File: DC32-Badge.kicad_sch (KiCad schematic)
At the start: 37 parts, among them J1 Conn_01x06, J2 Hirose_FH34-SRJ-24S, J3 Conn_01x06, J4 Conn_01x06, J5 Micro_SD_Card_Det, P1 2479, Q1 RTF025N03TL, SW1 SW_Push_DPDT, SW2 SW_Push_DPDT, SW3 SW_Push, SW4 SW_Push, U1 ESP32-C3-MINI-1, U2 AP2112K-3.3

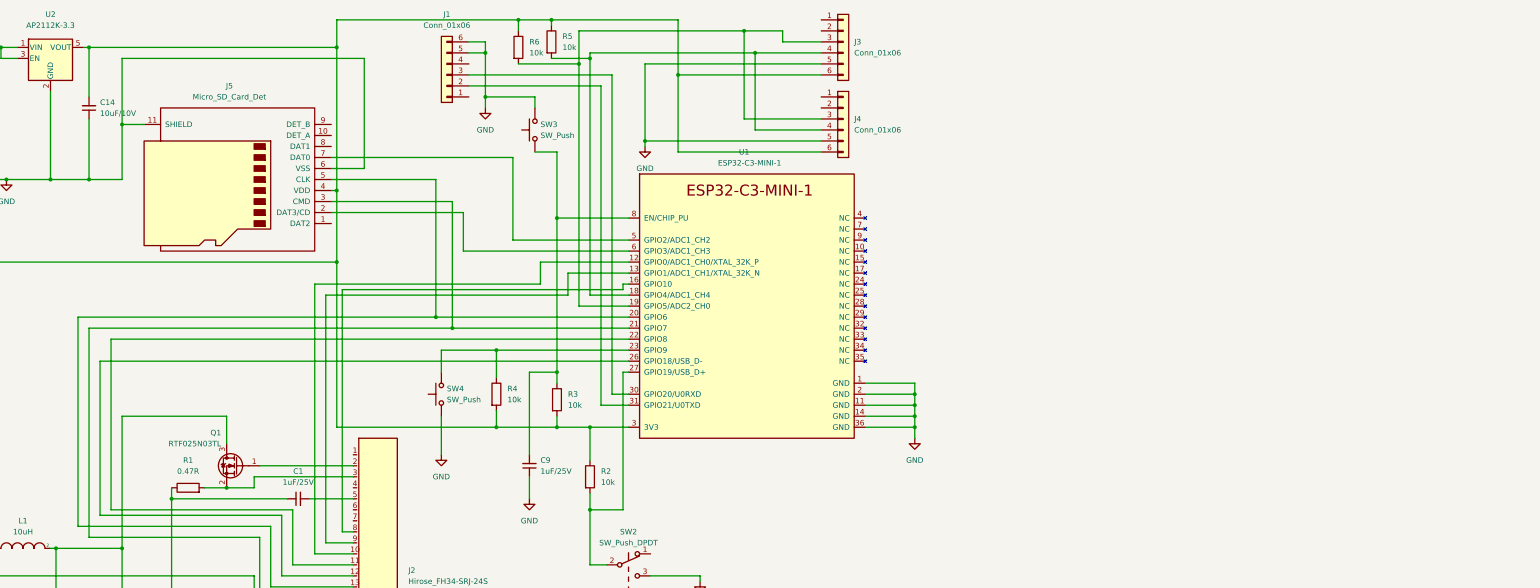
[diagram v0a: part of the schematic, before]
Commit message: Replaced ESP32-MINI with ESP32-WROOM in the kicad_sch file.
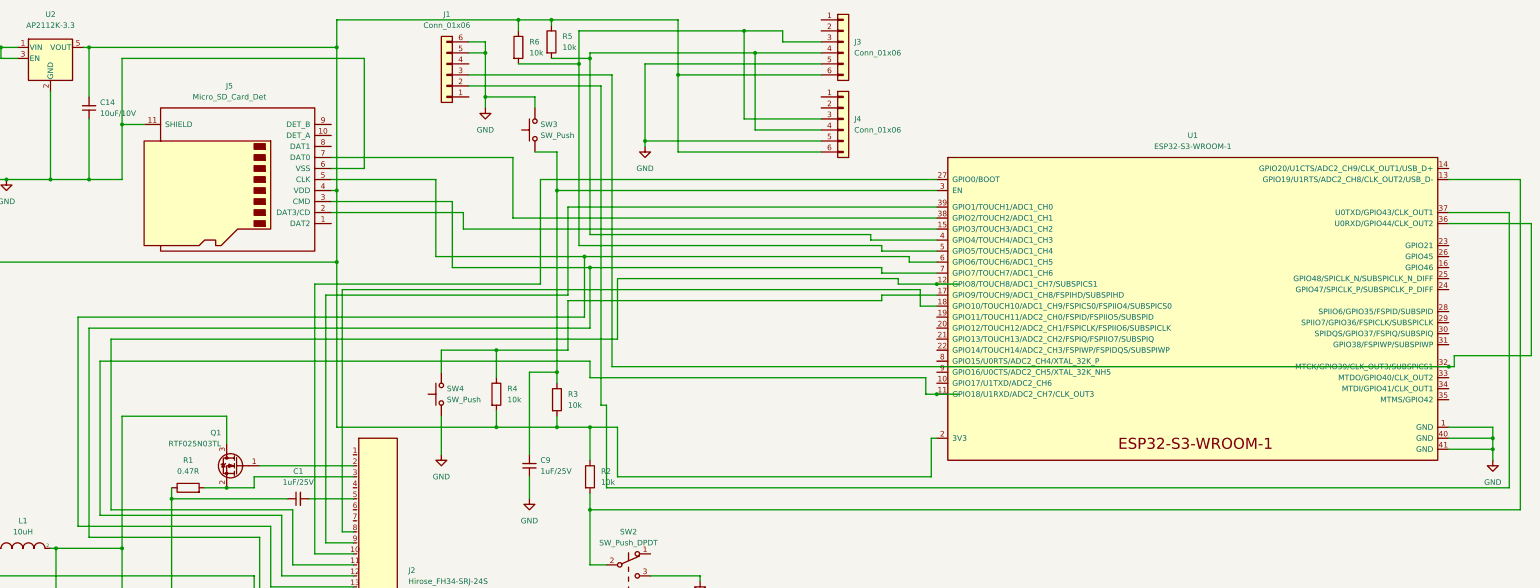
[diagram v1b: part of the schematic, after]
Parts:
- removed U1: ESP32-C3-MINI-1, Espressif:ESP32-C3-MINI-1, symbol Espressif:ESP32-C3-MINI-1
- added U1: ESP32-S3-WROOM-1, Espressif:ESP32-S3-WROOM-1, symbol Espressif:ESP32-S3-WROOM-1
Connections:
- net GND: now also U1.1 (GND), U1.40 (GND), U1.41 (GND)
- net at J1.2 (Pin_2): now also U1.37 (U0TXD/GPIO43/CLK_OUT1)
- net at J1.3 (Pin_3): now also U1.32 (MTCK/GPIO39/CLK_OUT3/SUBSPICS1), U1.36 (U0RXD/GPIO44/CLK_OUT2)
- net at C11.2, C14.2, C8.2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: now also U1.2 (3V3)
- net at J5.2 (DAT3/CD): now also U1.15 (GPIO3/TOUCH3/ADC1_CH2)
- net at J2.14, J5.3 (CMD): now also U1.7 (GPIO7/TOUCH7/ADC1_CH6)
- net at J2.13, J5.5 (CLK): now also U1.6 (GPIO6/TOUCH6/ADC1_CH5)
- net at J5.7 (DAT0): now also U1.38 (GPIO2/TOUCH2/ADC1_CH1)
- net at J2.10: now also U1.27 (GPIO0/BOOT)
- net at J2.9: now also U1.39 (GPIO1/TOUCH1/ADC1_CH0)
- net at J2.8: now also U1.18 (GPIO10/TOUCH10/ADC1_CH9/FSPICS0/FSPIIO4/SUBSPICS0)
- net at J3.4 (Pin_4), J4.4 (Pin_4), R5.2: now also U1.4 (GPIO4/TOUCH4/ADC1_CH3)
- net at J3.3 (Pin_3), J4.3 (Pin_3), R6.2: now also U1.5 (GPIO5/TOUCH5/ADC1_CH4)
- net at J2.11: now also U1.12 (GPIO8/TOUCH8/ADC1_CH7/SUBSPICS1)
- net at R4.1, SW4.2: now also U1.17 (GPIO9/TOUCH9/ADC1_CH8/FSPIHD/SUBSPIHD)
- net at J2.12: now also U1.11 (GPIO18/U1RXD/ADC2_CH7/CLK_OUT3)
- net at R2.2, SW2.2 (B): now also U1.13 (GPIO19/U1RTS/ADC2_CH8/CLK_OUT2/USB_D-)
- net at C9.2, R3.1, SW3.1: now also U1.3 (EN)

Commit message: Fit design on one page by modularizon. Added some button debouncing capacitors. Changed some of the GPIO pins.
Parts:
- added C15, C16: 1uF/25V, Capacitor_SMD:C_0603_1608Metric, symbol Device:C_Small
- SW2: value SW_Push_DPDT -> EVIL_SWITCH
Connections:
- net GND: now also C15.1, C16.1
- net PROG_TX: now reaches J1.2 (Pin_2), U1.37 (U0TXD/GPIO43/CLK_OUT1)
- net PROG_RX: now reaches J1.3 (Pin_3), U1.36 (U0RXD/GPIO44/CLK_OUT2)
- net PROG_RX: no longer U1.32 (MTCK/GPIO39/CLK_OUT3/SUBSPICS1)
- net +3.3V: now reaches C11.2, C14.2, C8.2, J2.15, J2.16, J3.6 (Pin_6), J4.6 (Pin_6), J5.4 (VDD), L1.1, R2.1, R5.1, R6.1, U1.2 (3V3), U2.5 (VOUT)
- net +3.3V: now also R3.1, R4.1; no longer R3.2, R4.2
- net RST: now reaches C9.2, SW3.1, U1.3 (EN)
- net RST: now also R3.2; no longer R3.1
- net SDA: now reaches J3.3 (Pin_3), J4.3 (Pin_3), R6.2, U1.5 (GPIO5/TOUCH5/ADC1_CH4)
- net SCL: now reaches J3.4 (Pin_4), J4.4 (Pin_4), R5.2, U1.4 (GPIO4/TOUCH4/ADC1_CH3)
- net at U1.12 (GPIO8/TOUCH8/ADC1_CH7/SUBSPICS1): no longer J2.11
- net EVIL: now reaches R2.2, SW2.2 (B), U1.13 (GPIO19/U1RTS/ADC2_CH8/CLK_OUT2/USB_D-)
- net EVIL: now also C16.2
- net SW_PUSH: now reaches SW4.2, U1.17 (GPIO9/TOUCH9/ADC1_CH8/FSPIHD/SUBSPIHD)
- net SW_PUSH: now also R4.2, C15.2; no longer R4.1
- net at U1.19 (GPIO11/TOUCH11/ADC2_CH0/FSPID/FSPIIO5/SUBSPID): now also J2.9
- net at U1.20 (GPIO12/TOUCH12/ADC2_CH1/FSPICLK/FSPIIO6/SUBSPICLK): now also J2.10
- net at U1.21 (GPIO13/TOUCH13/ADC2_CH2/FSPIQ/FSPIIO7/SUBSPIQ): now also J2.11
- net at U1.27 (GPIO0/BOOT): no longer J2.10
- net at U1.39 (GPIO1/TOUCH1/ADC1_CH0): no longer J2.9
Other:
- moved on the sheet: C1, C10, C13, C14, C9, J1, J2, J3, J4, J5, P1, Q1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

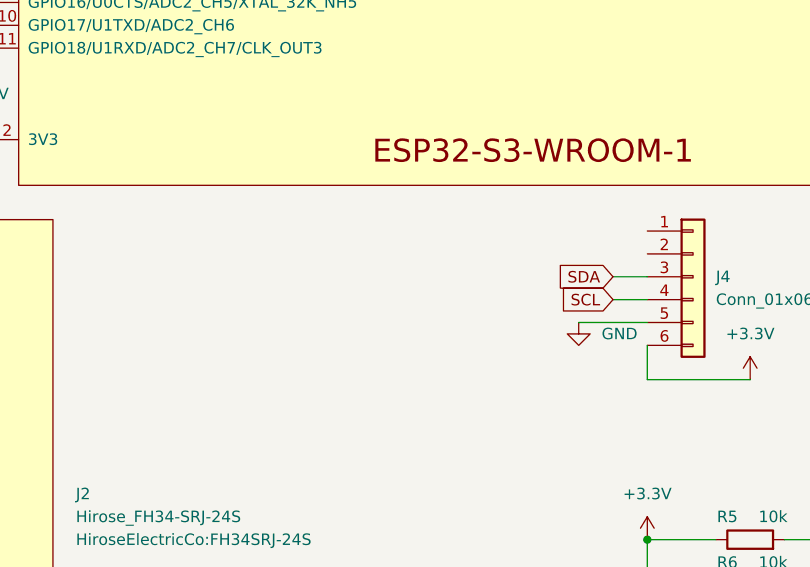
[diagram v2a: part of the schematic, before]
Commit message: Added third SAO port.
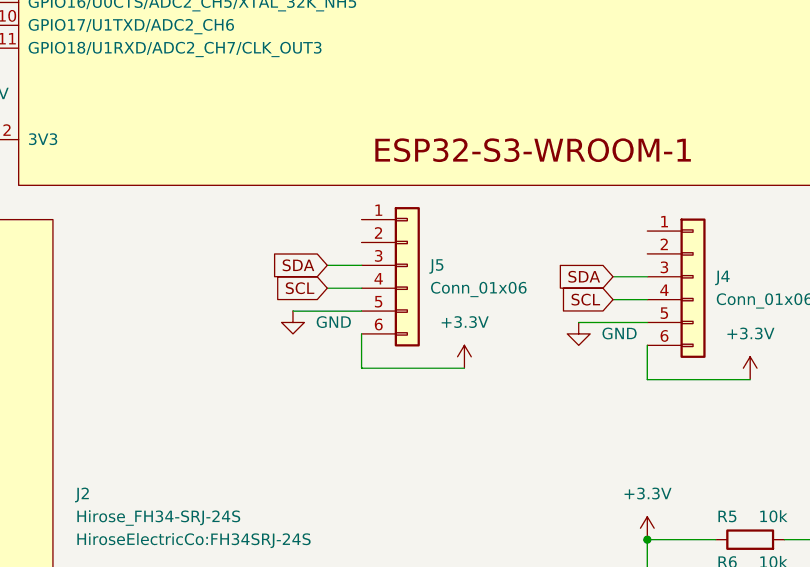
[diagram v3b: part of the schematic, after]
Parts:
- added J5: Conn_01x06, Connector_PinSocket_2.54mm:PinSocket_2x03_P2.54mm_Vertical_SMD, symbol Connector_Generic:Conn_01x06
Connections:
- net +3.3V: now also J5.6 (Pin_6)
- net GND: now also J5.5 (Pin_5)
- net SCL: now also J5.4 (Pin_4)
- net SDA: now also J5.3 (Pin_3)
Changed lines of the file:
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@@
+    (stroke (width 0) (type default) (color 0 0 0 0))
+  )
+  (wire (pts (xy 190.5 124.46) (xy 190.5 128.27))
     (stroke (width 0) (type default) (color 0 0 0 0))
   )
@@
     (stroke (width 0) (type default) (color 0 0 0 0))
   )
+  (wire (pts (xy 186.69 119.38) (xy 190.5 119.38))
+    (stroke (width 0) (type default) (color 0 0 0 0))
+  )
   (wire (pts (xy 30.48 113.03) (xy 34.29 113.03))
     (stroke (width 0) (type default) (color 0 0 0 0))
@@
     (stroke (width 0) (type default) (color 0 0 0 0))
   )
+  (wire (pts (xy 201.93 128.27) (xy 190.5 128.27))
+    (stroke (width 0) (type default) (color 0 0 0 0))
+  )
   (wire (pts (xy 143.51 171.45) (xy 143.51 181.61))
     (stroke (width 0) (type default) (color 0 0 0 0))
@@
     (stroke (width 0) (type default) (color 0 0 0 0))
   )
+  (wire (pts (xy 182.88 121.92) (xy 190.5 121.92))
+    (stroke (width 0) (type default) (color 0 0 0 0))
+  )
   (wire (pts (xy 29.21 110.49) (xy 29.21 107.95))
     (stroke (width 0) (type default) (color 0 0 0 0))
@@
   )
   (wire (pts (xy 140.97 153.67) (xy 140.97 151.13))
+    (stroke (width 0) (type default) (color 0 0 0 0))
+  )
+  (wire (pts (xy 186.69 116.84) (xy 190.5 116.84))
     (stroke (width 0) (type default) (color 0 0 0 0))
   )
@@
     )
   )
+  (global_label "SCL" (shape input) (at 186.69 119.38 180) (fields_autoplaced)
+    (effects (font (size 1.27 1.27)) (justify right))
+    (property "Intersheet References" "${INTERSHEET_REFS}" (id 0) (at 180.7693 119.3006 0)
+      (effects (font (size 1.27 1.27)) (justify right) hide)
+    )
+  )
   (global_label "RST" (shape input) (at 144.78 45.72 180) (fields_autoplaced)
     (effects (font (size 1.27 1.27)) (justify right))
@@
     (effects (font (size 1.27 1.27)) (justify right))
     (property "Intersheet References" "${INTERSHEET_REFS}" (id 0) (at 212.4588 118.0306 0)
+      (effects (font (size 1.27 1.27)) (justify right) hide)
+    )
+  )
+  (global_label "SDA" (shape input) (at 186.69 116.84 180) (fields_autoplaced)
+    (effects (font (size 1.27 1.27)) (justify right))
+    (property "Intersheet References" "${INTERSHEET_REFS}" (id 0) (at 180.7088 116.7606 0)
       (effects (font (size 1.27 1.27)) (justify right) hide)
     )
@@
     (pin "2")
   )
+  (symbol (lib_id "power:GND") (at 182.88 121.92 0) (unit 1)
+    (in_bom yes) (on_board yes) (fields_autoplaced)
+    (property "Reference" "#PWR?" (id 0) (at 182.88 128.27 0)
+      (effects (font (size 1.27 1.27)) hide)
+    )
+    (property "Value" "GND" (id 1) (at 185.42 123.1899 0)
+      (effects (font (size 1.27 1.27)) (justify left))
+    )
+    (property "Footprint" "" (id 2) (at 182.88 121.92 0)
+      (effects (font (size 1.27 1.27)) hide)
+    )
+    (property "Datasheet" "" (id 3) (at 182.88 121.92 0)
+      (effects (font (size 1.27 1.27)) hide)
+    )
+    (pin "1")
+  )
   (symbol (lib_id "power:GND") (at 246.38 124.46 0) (unit 1)
     (in_bom yes) (on_board yes) (fields_autoplaced)
@@
     (pin "1")
   )
+  (symbol (lib_id "power:+3.3V") (at 201.93 128.27 0) (unit 1)
+    (in_bom yes) (on_board yes) (fields_autoplaced)
+    (property "Reference" "#PWR?" (id 0) (at 201.93 132.08 0)
+      (effects (font (size 1.27 1.27)) hide)
+    )
+    (property "Value" "+3.3V" (id 1) (at 201.93 123.19 0))
+    (property "Footprint" "" (id 2) (at 201.93 128.27 0)
+      (effects (font (size 1.27 1.27)) hide)
+    )
+    (property "Datasheet" "" (id 3) (at 201.93 128.27 0)
+      (effects (font (size 1.27 1.27)) hide)
+    )
+    (pin "1")
+  )
   (symbol (lib_id "Device:D_Zener") (at 96.52 152.4 90) (unit 1)
     (in_bom yes) (on_board yes)
@@
     (pin "5")
   )
+  (symbol (lib_id "Connector_Generic:Conn_01x06") (at 195.58 116.84 0) (unit 1)
+    (in_bom yes) (on_board yes) (fields_autoplaced)
+    (property "Reference" "J5" (id 0) (at 198.12 116.8399 0)
+      (effects (font (size 1.27 1.27)) (justify left))
+    )
+    (property "Value" "Conn_01x06" (id 1) (at 198.12 119.3799 0)
+      (effects (font (size 1.27 1.27)) (justify left))
+    )
+    (property "Footprint" "Connector_PinSocket_2.54mm:PinSocket_2x03_P2.54mm_Vertical_SMD" (id 2) (at 195.58 116.84 0)
+      (effects (font (size 1.27 1.27)) hide)
+    )
+    (property "Datasheet" "~" (id 3) (at 195.58 116.84 0)
+      (effects (font (size 1.27 1.27)) hide)
+    )
+    (pin "1")
+    (pin "2")
+    (pin "3")
+    (pin "4")
+    (pin "5")
+    (pin "6")
+  )
   (sheet_instances
     (path "/" (page "1"))
@@
       (reference "#PWR?") (unit 1) (value "+3.3V") (footprint "")
     )
+    (path "/95757e6a-4ef9-4af1-bfcc-a5c94f1e0ac1"
+      (reference "#PWR?") (unit 1) (value "GND") (footprint "")
+    )
     (path "/9d5478b3-5869-4fce-95d0-677535665a0c"
       (reference "#PWR?") (unit 1) (value "GND") (footprint "")
@@
       (reference "#PWR?") (unit 1) (value "GND") (footprint "")
     )
+    (path "/ea8c9e6f-2fcf-4b97-821a-7bdc1d660d02"
+      (reference "#PWR?") (unit 1) (value "+3.3V") (footprint "")
+    )
     (path "/f96b0acd-244e-4a03-9920-357dc41b964a"
       (reference "#PWR?") (unit 1) (value "+3.3V") (footprint "")
@@
       (reference "J5") (unit 1) (value "Micro_SD_Card_Det") (footprint "Connector_Card:microSD_HC_Hirose_DM3AT-SF-PEJM5")
     )
+    (path "/fcf93aac-f8fb-4d4c-9782-4e9681b41fa9"
+      (reference "J5") (unit 1) (value "Conn_01x06") (footprint "Connector_PinSocket_2.54mm:PinSocket_2x03_P2.54mm_Vertical_SMD")
+    )
     (path "/42d325ad-d3be-4805-86d4-f0013e4e1acd"

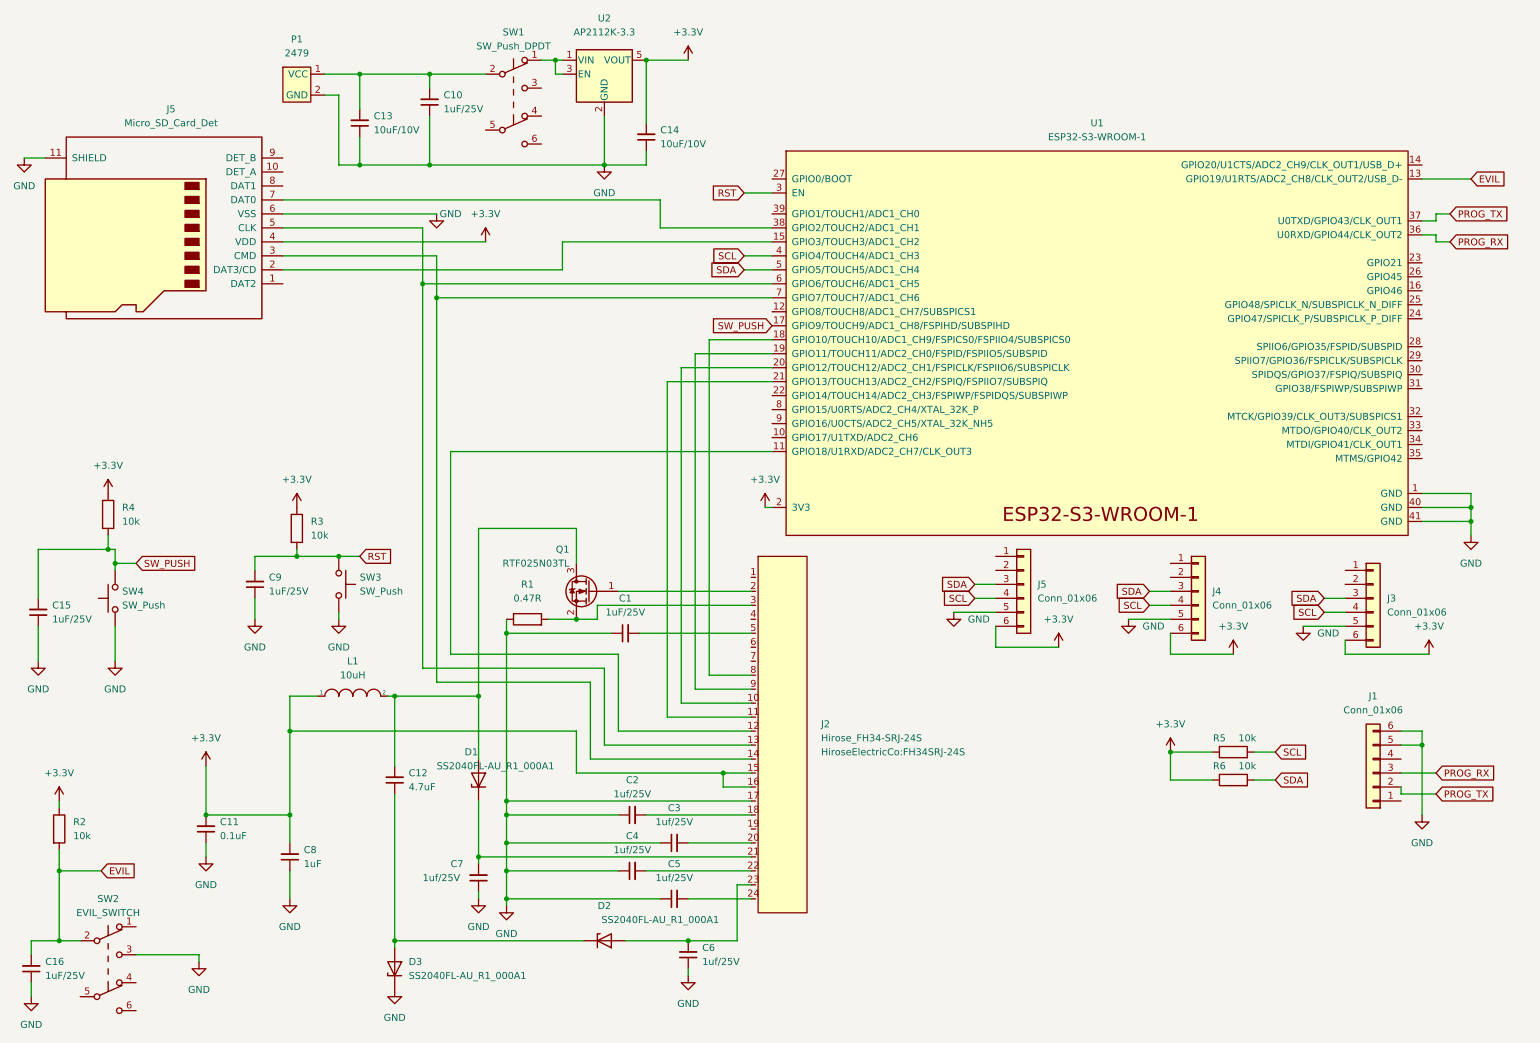
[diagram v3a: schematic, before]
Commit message: Rearranged some pins. Added a PROGRAM switch.
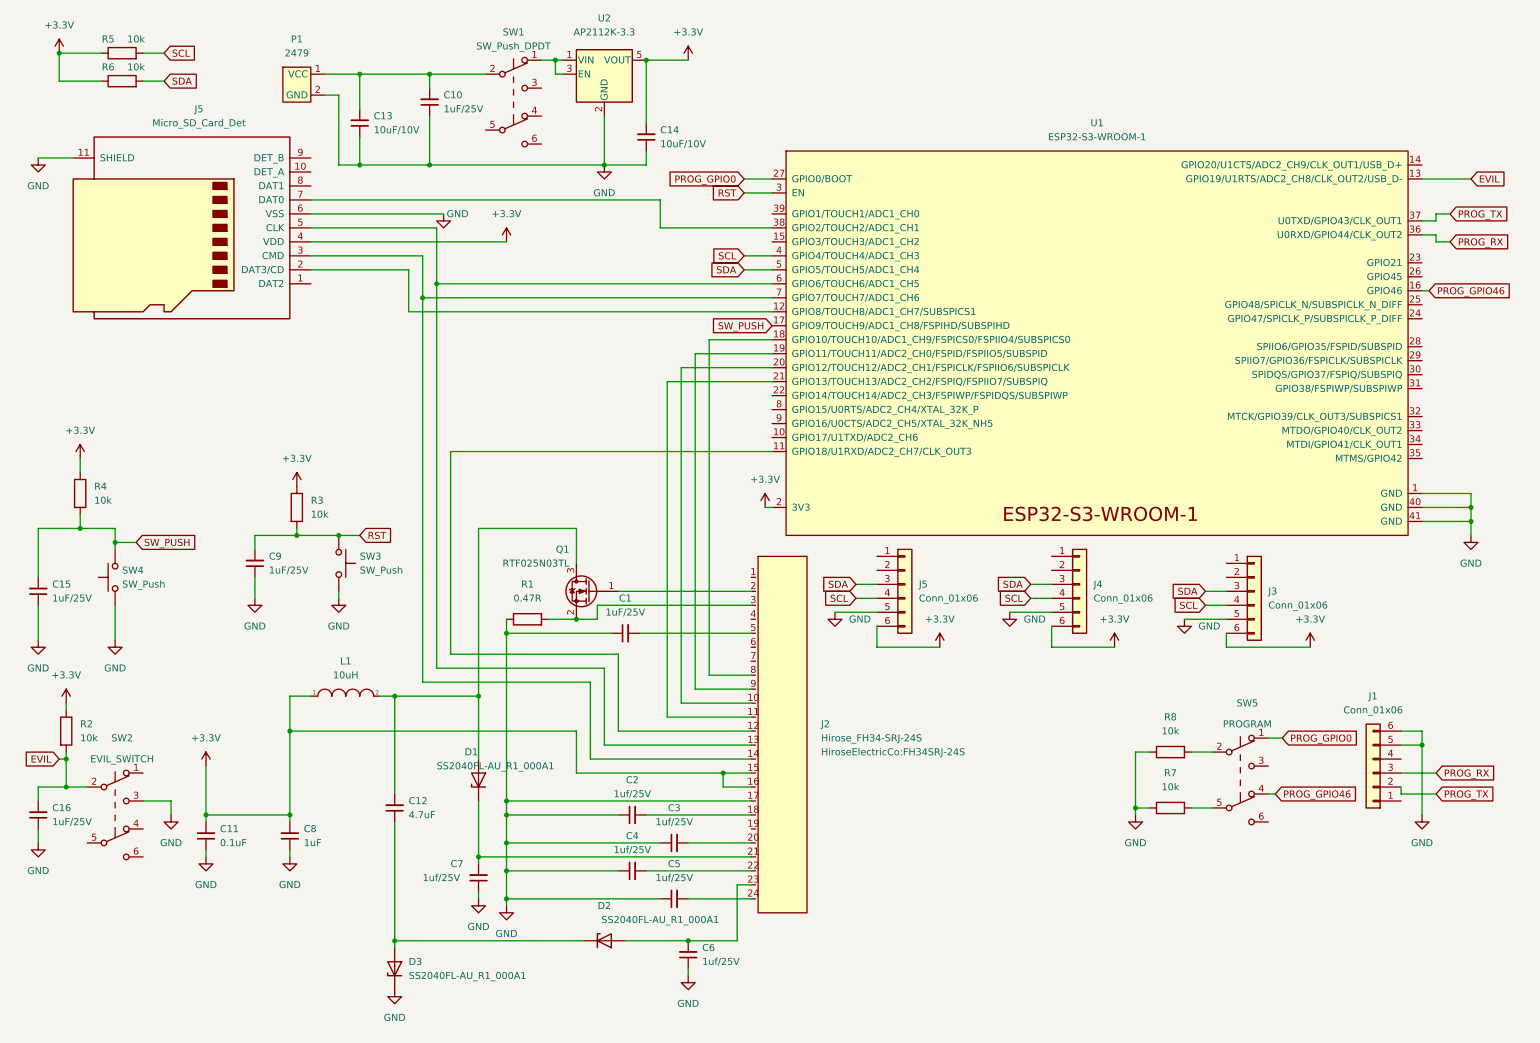
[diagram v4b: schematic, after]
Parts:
- added R7, R8: 10k, Resistor_SMD:R_0603_1608Metric, symbol Device:R
- added SW5: PROGRAM, Button_Switch_THT:SW_E-Switch_EG1271_SPDT, symbol Switch:SW_Push_DPDT
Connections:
- net GND: now also R7.1, R8.1
- net at J5.2 (DAT3/CD): now also U1.12 (GPIO8/TOUCH8/ADC1_CH7/SUBSPICS1); no longer U1.15 (GPIO3/TOUCH3/ADC1_CH2)
- net PROG_GPIO46: now reaches U1.16 (GPIO46)
- net PROG_GPIO46: now also SW5.4 (A)
- net PROG_GPIO0: now reaches U1.27 (GPIO0/BOOT)
- net PROG_GPIO0: now also SW5.1 (A)
- new net: R8.2, SW5.2 (B)
- new net: R7.2, SW5.5 (B)
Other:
- moved on the sheet: C11, C12, C15, C16, C8, C9, J3, J4, J5, L1, R2, R3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
